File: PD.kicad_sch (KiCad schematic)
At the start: 7 parts, among them U3 AD8603

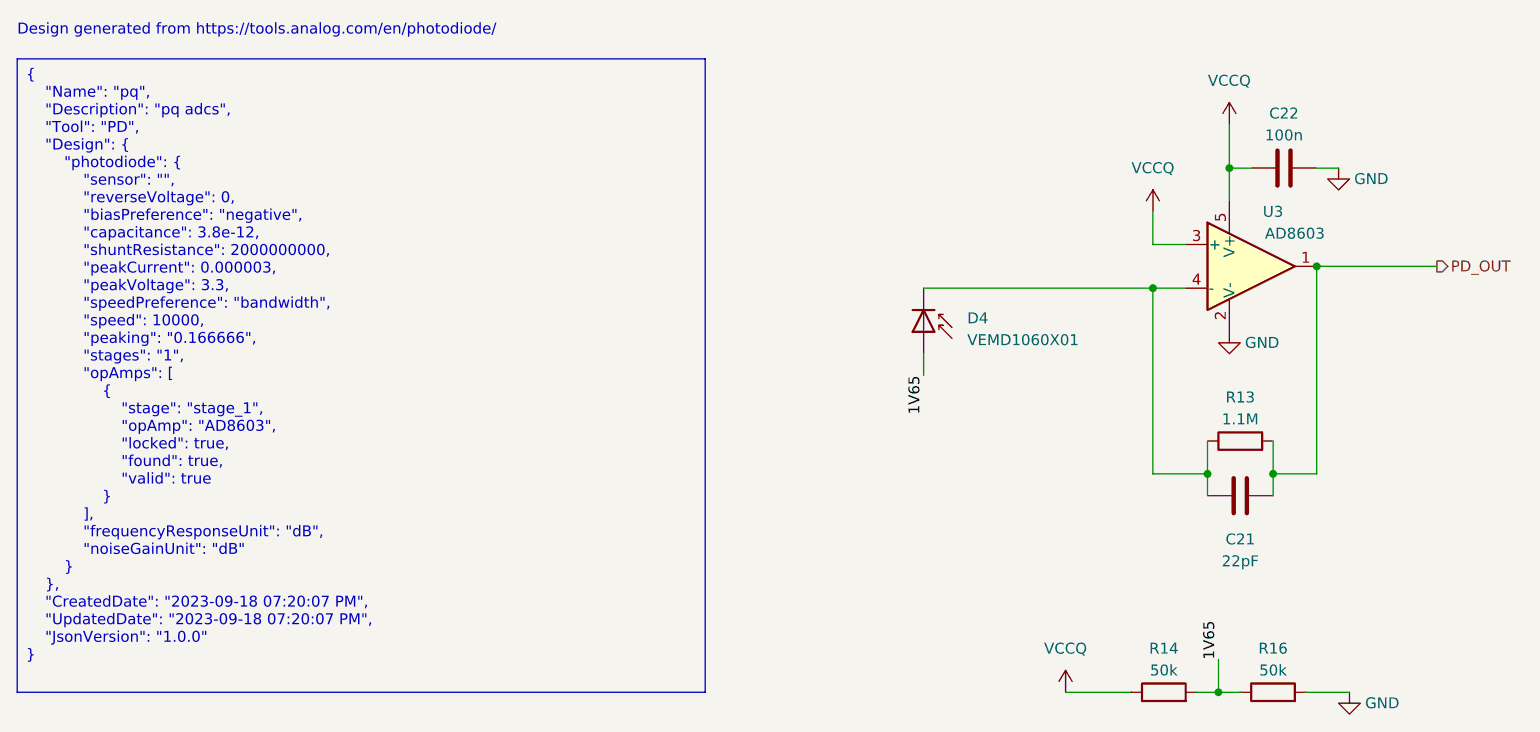
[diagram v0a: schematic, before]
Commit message: Reannotate schematic
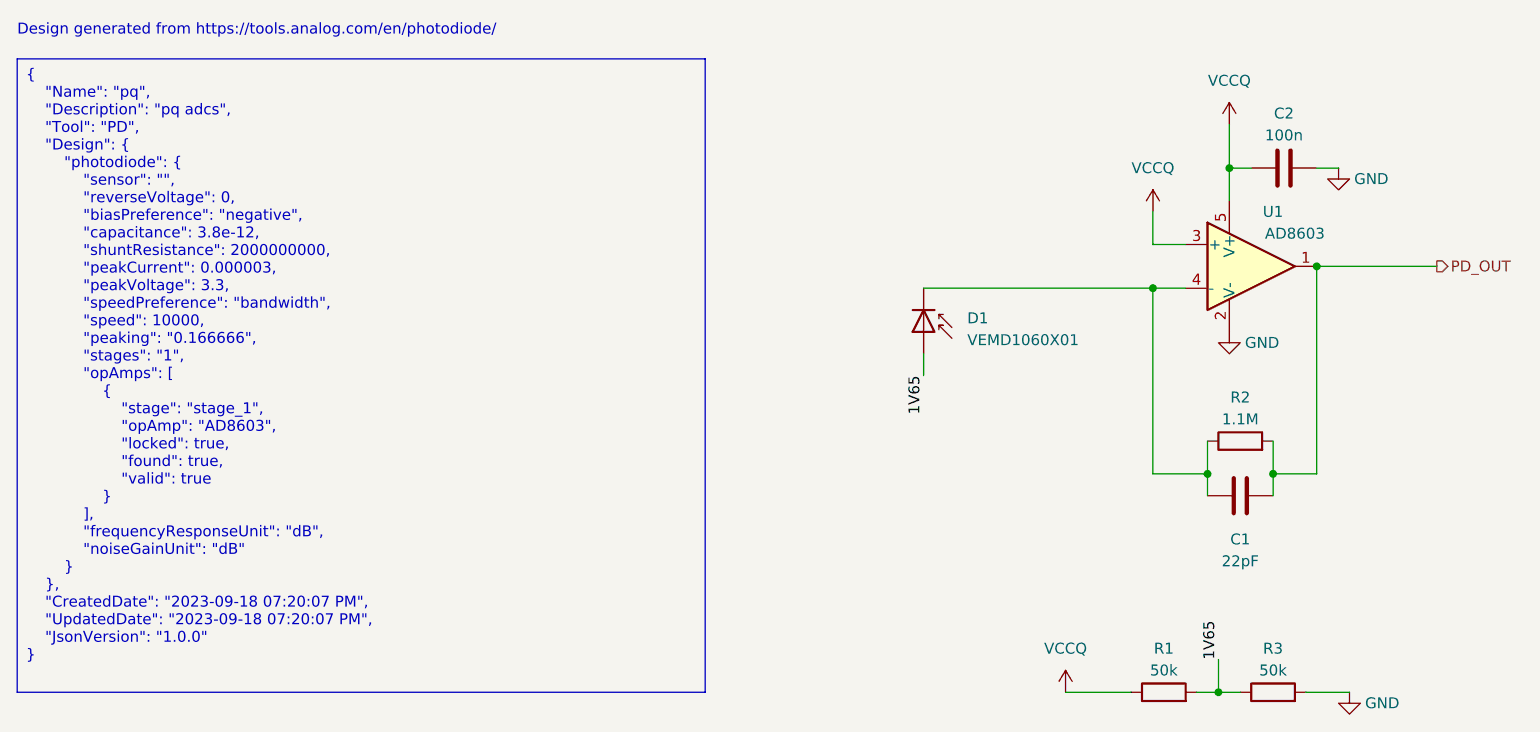
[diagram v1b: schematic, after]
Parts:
- renumbered C21 to C1, C22 to C2, D4 to D1, R14 to R1, R13 to R2, R16 to R3, U3 to U1
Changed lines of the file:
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@@
   (symbol (lib_id "power:VCCQ") (at 167.64 92.71 0) (unit 1)
     (in_bom yes) (on_board yes) (dnp no)
-    (property "Reference" "#PWR071" (at 167.64 96.52 0)
+    (property "Reference" "#PWR04" (at 167.64 96.52 0)
       (effects (font (size 1.27 1.27)) hide)
     )
@@
       (project "NEW_PCB_ADCS"
         (path "/42c40d7d-71af-4ce9-bac9-d638f259c957/c29ef61c-00a4-4c47-8fd5-831f174cebbb"
-          (reference "#PWR071") (unit 1)
+          (reference "#PWR04") (unit 1)
         )
       )
@@
   (symbol (lib_id "power:VCCQ") (at 157.48 148.59 0) (unit 1)
     (in_bom yes) (on_board yes) (dnp no)
-    (property "Reference" "#PWR072" (at 157.48 152.4 0)
+    (property "Reference" "#PWR03" (at 157.48 152.4 0)
       (effects (font (size 1.27 1.27)) hide)
     )
@@
       (project "NEW_PCB_ADCS"
         (path "/42c40d7d-71af-4ce9-bac9-d638f259c957/c29ef61c-00a4-4c47-8fd5-831f174cebbb"
-          (reference "#PWR072") (unit 1)
+          (reference "#PWR03") (unit 1)
         )
       )
@@
   (symbol (lib_id "power:GND") (at 189.23 87.63 0) (unit 1)
     (in_bom yes) (on_board yes) (dnp no)
-    (property "Reference" "#PWR070" (at 189.23 93.98 0)
+    (property "Reference" "#PWR07" (at 189.23 93.98 0)
       (effects (font (size 1.27 1.27)) hide)
     )
@@
       (project "NEW_PCB_ADCS"
         (path "/42c40d7d-71af-4ce9-bac9-d638f259c957/c29ef61c-00a4-4c47-8fd5-831f174cebbb"
-          (reference "#PWR070") (unit 1)
+          (reference "#PWR07") (unit 1)
         )
       )
@@
   (symbol (lib_id "Amplifier_Operational:AD8603") (at 179.07 99.06 0) (unit 1)
     (in_bom yes) (on_board yes) (dnp no)
-    (property "Reference" "U3" (at 181.61 92.71 0)
+    (property "Reference" "U1" (at 181.61 92.71 0)
       (effects (font (size 1.27 1.27)))
     )
@@
       (project "NEW_PCB_ADCS"
         (path "/42c40d7d-71af-4ce9-bac9-d638f259c957/c29ef61c-00a4-4c47-8fd5-831f174cebbb"
-          (reference "U3") (unit 1)
+          (reference "U1") (unit 1)
         )
       )
@@
   (symbol (lib_id "Device:D_Photo") (at 140.97 106.68 270) (unit 1)
     (in_bom yes) (on_board yes) (dnp no) (fields_autoplaced)
-    (property "Reference" "D4" (at 146.05 105.0925 90)
+    (property "Reference" "D1" (at 146.05 105.0925 90)
       (effects (font (size 1.27 1.27)) (justify left))
     )
@@
       (project "NEW_PCB_ADCS"
         (path "/42c40d7d-71af-4ce9-bac9-d638f259c957/c29ef61c-00a4-4c47-8fd5-831f174cebbb"
-          (reference "D4") (unit 1)
+          (reference "D1") (unit 1)
         )
       )
@@
   (symbol (lib_id "Device:C") (at 177.8 125.73 270) (unit 1)
     (in_bom yes) (on_board yes) (dnp no) (fields_autoplaced)
-    (property "Reference" "C21" (at 177.8 130.81 90)
+    (property "Reference" "C1" (at 177.8 130.81 90)
       (effects (font (size 1.27 1.27)))
     )
@@
       (project "NEW_PCB_ADCS"
         (path "/42c40d7d-71af-4ce9-bac9-d638f259c957/c29ef61c-00a4-4c47-8fd5-831f174cebbb"
-          (reference "C21") (unit 1)
+          (reference "C1") (unit 1)
         )
       )
@@
   (symbol (lib_id "power:GND") (at 176.53 106.68 0) (unit 1)
     (in_bom yes) (on_board yes) (dnp no)
-    (property "Reference" "#PWR068" (at 176.53 113.03 0)
+    (property "Reference" "#PWR06" (at 176.53 113.03 0)
       (effects (font (size 1.27 1.27)) hide)
     )
@@
       (project "NEW_PCB_ADCS"
         (path "/42c40d7d-71af-4ce9-bac9-d638f259c957/c29ef61c-00a4-4c47-8fd5-831f174cebbb"
-          (reference "#PWR068") (unit 1)
+          (reference "#PWR06") (unit 1)
         )
       )
@@
   (symbol (lib_id "Device:R") (at 177.8 119.38 90) (unit 1)
     (in_bom yes) (on_board yes) (dnp no) (fields_autoplaced)
-    (property "Reference" "R13" (at 177.8 114.3 90)
+    (property "Reference" "R2" (at 177.8 114.3 90)
       (effects (font (size 1.27 1.27)))
     )
@@
       (project "NEW_PCB_ADCS"
         (path "/42c40d7d-71af-4ce9-bac9-d638f259c957/c29ef61c-00a4-4c47-8fd5-831f174cebbb"
-          (reference "R13") (unit 1)
+          (reference "R2") (unit 1)
         )
       )
@@
   (symbol (lib_id "Device:R") (at 168.91 148.59 90) (unit 1)
     (in_bom yes) (on_board yes) (dnp no) (fields_autoplaced)
-    (property "Reference" "R14" (at 168.91 143.51 90)
+    (property "Reference" "R1" (at 168.91 143.51 90)
       (effects (font (size 1.27 1.27)))
     )
@@
       (project "NEW_PCB_ADCS"
         (path "/42c40d7d-71af-4ce9-bac9-d638f259c957/c29ef61c-00a4-4c47-8fd5-831f174cebbb"
-          (reference "R14") (unit 1)
+          (reference "R1") (unit 1)
         )
       )
@@
   (symbol (lib_id "power:VCCQ") (at 176.53 82.55 0) (unit 1)
     (in_bom yes) (on_board yes) (dnp no)
-    (property "Reference" "#PWR069" (at 176.53 86.36 0)
+    (property "Reference" "#PWR05" (at 176.53 86.36 0)
       (effects (font (size 1.27 1.27)) hide)
     )
@@
       (project "NEW_PCB_ADCS"
         (path "/42c40d7d-71af-4ce9-bac9-d638f259c957/c29ef61c-00a4-4c47-8fd5-831f174cebbb"
-          (reference "#PWR069") (unit 1)
+          (reference "#PWR05") (unit 1)
         )
       )
@@
   (symbol (lib_id "power:GND") (at 190.5 148.59 0) (unit 1)
     (in_bom yes) (on_board yes) (dnp no)
-    (property "Reference" "#PWR073" (at 190.5 154.94 0)
+    (property "Reference" "#PWR08" (at 190.5 154.94 0)
       (effects (font (size 1.27 1.27)) hide)
     )
@@
       (project "NEW_PCB_ADCS"
         (path "/42c40d7d-71af-4ce9-bac9-d638f259c957/c29ef61c-00a4-4c47-8fd5-831f174cebbb"
-          (reference "#PWR073") (unit 1)
+          (reference "#PWR08") (unit 1)
         )
       )
@@
   (symbol (lib_id "Device:R") (at 181.61 148.59 90) (unit 1)
     (in_bom yes) (on_board yes) (dnp no) (fields_autoplaced)
-    (property "Reference" "R16" (at 181.61 143.51 90)
+    (property "Reference" "R3" (at 181.61 143.51 90)
       (effects (font (size 1.27 1.27)))
     )
@@
       (project "NEW_PCB_ADCS"
         (path "/42c40d7d-71af-4ce9-bac9-d638f259c957/c29ef61c-00a4-4c47-8fd5-831f174cebbb"
-          (reference "R16") (unit 1)
+          (reference "R3") (unit 1)
         )
       )
@@
   (symbol (lib_id "Device:C") (at 182.88 87.63 90) (unit 1)
     (in_bom yes) (on_board yes) (dnp no) (fields_autoplaced)
-    (property "Reference" "C22" (at 182.88 81.28 90)
+    (property "Reference" "C2" (at 182.88 81.28 90)
       (effects (font (size 1.27 1.27)))
     )
@@
       (project "NEW_PCB_ADCS"
         (path "/42c40d7d-71af-4ce9-bac9-d638f259c957/c29ef61c-00a4-4c47-8fd5-831f174cebbb"
-          (reference "C22") (unit 1)
-        )
-      )
+          (reference "C2") (unit 1)
+        )
+      )

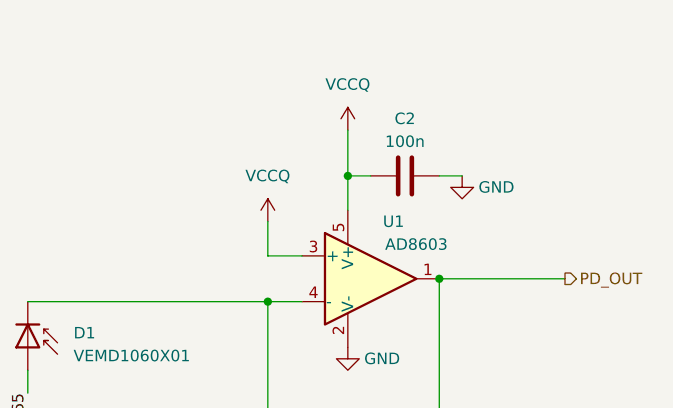
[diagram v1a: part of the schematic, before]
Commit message: Create PCB layout and routing
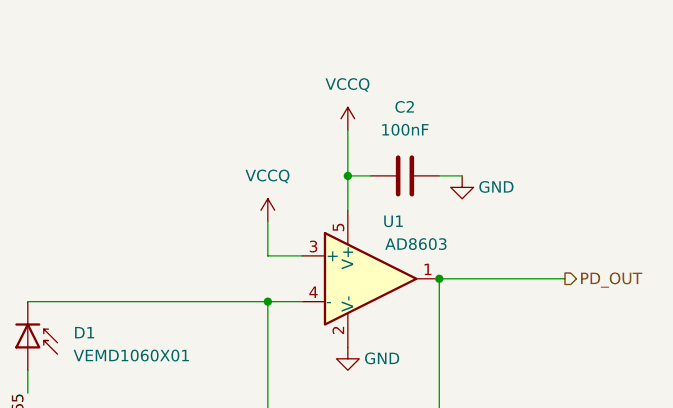
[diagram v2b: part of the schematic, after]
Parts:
- C2: value 100n -> 100nF; footprint (none) -> Capacitor_SMD:C_0603_1608Metric
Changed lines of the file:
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@@
   (symbol (lib_id "Device:C") (at 182.88 87.63 90) (unit 1)
     (in_bom yes) (on_board yes) (dnp no) (fields_autoplaced)
-    (property "Reference" "C2" (at 182.88 81.28 90)
+    (property "Reference" "C2" (at 182.88 80.01 90)
       (effects (font (size 1.27 1.27)))
     )
-    (property "Value" "100n" (at 182.88 83.82 90)
+    (property "Value" "100nF" (at 182.88 82.55 90)
       (effects (font (size 1.27 1.27)))
     )
-    (property "Footprint" "" (at 186.69 86.6648 0)
+    (property "Footprint" "Capacitor_SMD:C_0603_1608Metric" (at 186.69 86.6648 0)
       (effects (font (size 1.27 1.27)) hide)
     )

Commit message: Update some part numbers
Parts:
- C2: Part Number (none) -> C0603C104K9RACTU
- D1: Part Number (none) -> VEMD1060X01
- R1, R3: Part Number (none) -> RT0603BRD0750KL
- R2: Part Number (none) -> AC0603FR-071M1L
- U1: Part Number (none) -> AD8603AUJZ-REEL
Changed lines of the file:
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@@
+      (effects (font (size 1.27 1.27)) hide)
+    )
+    (property "Part Number" "AD8603AUJZ-REEL" (at 179.07 99.06 0)
       (effects (font (size 1.27 1.27)) hide)
     )
@@
     )
     (property "MPN" "VEMD1060X01" (at 140.97 106.68 0)
+      (effects (font (size 1.27 1.27)) hide)
+    )
+    (property "Part Number" "VEMD1060X01" (at 140.97 106.68 0)
       (effects (font (size 1.27 1.27)) hide)
     )
@@
       (effects (font (size 1.27 1.27)) hide)
     )
+    (property "Part Number" "AC0603FR-071M1L" (at 177.8 119.38 0)
+      (effects (font (size 1.27 1.27)) hide)
+    )
     (pin "1")
     (pin "2")
@@
     )
     (property "Datasheet" "~" (at 168.91 148.59 0)
+      (effects (font (size 1.27 1.27)) hide)
+    )
+    (property "Part Number" "RT0603BRD0750KL" (at 168.91 148.59 0)
       (effects (font (size 1.27 1.27)) hide)
     )
@@
       (effects (font (size 1.27 1.27)) hide)
     )
+    (property "Part Number" "RT0603BRD0750KL" (at 181.61 148.59 0)
+      (effects (font (size 1.27 1.27)) hide)
+    )
     (pin "1")
     (pin "2")
@@
       (effects (font (size 1.27 1.27)) hide)
     )
+    (property "Part Number" "C0603C104K9RACTU" (at 182.88 87.63 0)
+      (effects (font (size 1.27 1.27)) hide)
+    )
